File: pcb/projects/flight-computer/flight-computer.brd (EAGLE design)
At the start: 101.6 x 60.6 mm, 83 parts, among them IC1 ADG609RU, IC3 ADG609RU, P1 53048-0810, P2 53048-0810, U1 MCP73831/OT, U12 MAX31856MUD+, U13 MAX31856MUD+, U2 LP2985IM5-1.8/NOPB, U3 COM-13909, U4 ADXL377, U5 ICM-20948, U6 PCA9306DCUR, U7 SN74LVC1T45DRLR, U8 SN74LVC1T45DRLR, U9 DMP3099L

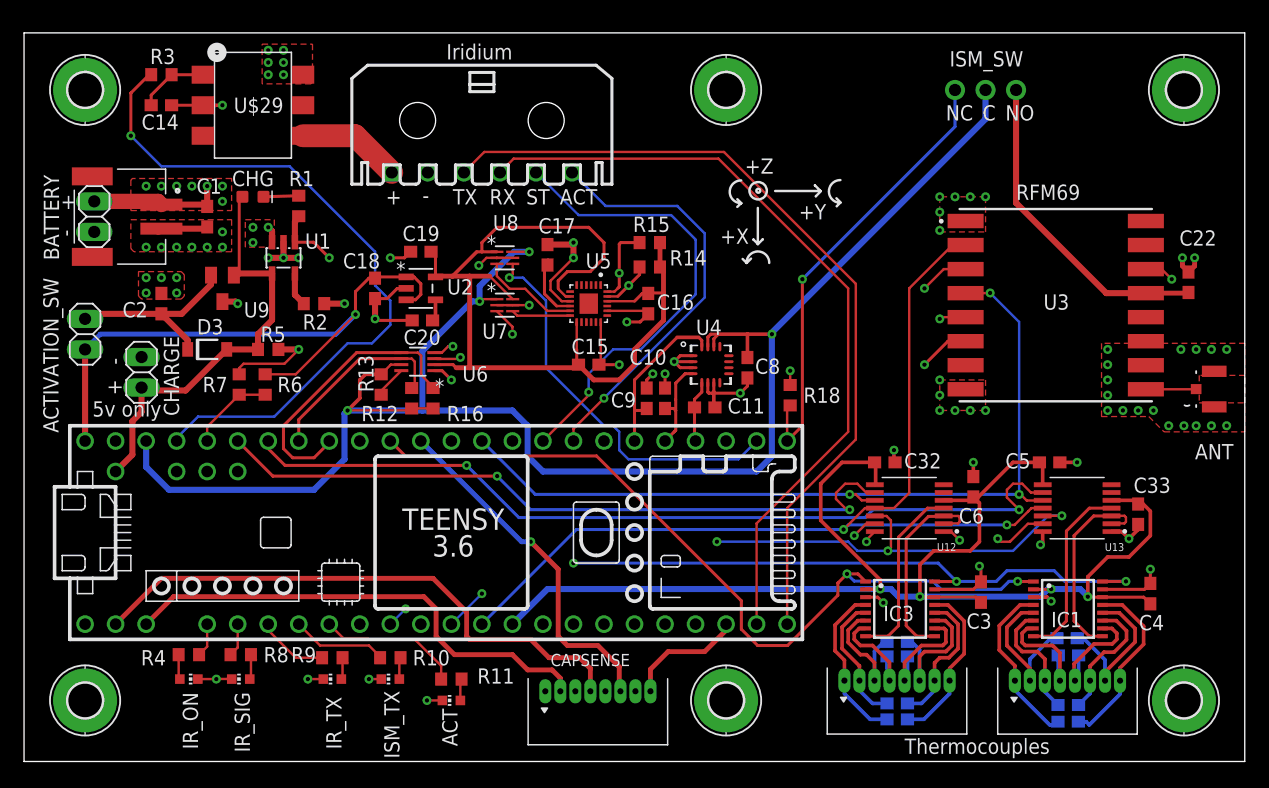
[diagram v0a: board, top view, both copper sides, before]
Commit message: add activation redundancy processor
- partial update of documentation to reflect this addition
- extra diagram of redundant activation
- pcb update to include a 32 pin qfn samd21 cortex m0 processor and necessary connections to bootload and flash over USB
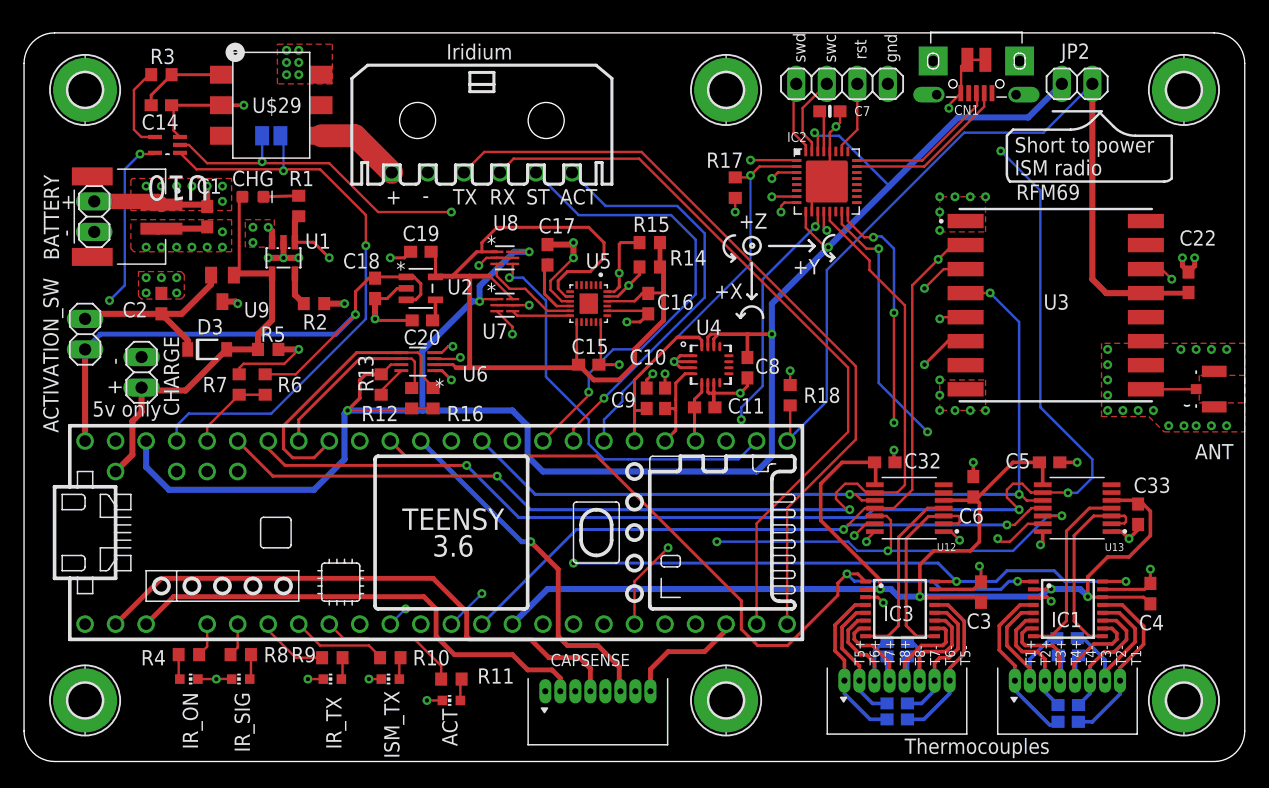
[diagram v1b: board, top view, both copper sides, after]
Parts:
- removed ISM_SW: (no value), adafruit:1X03-CLEANBIG
- added C7: 1uF, microbuilder:0603-NO
- added CN1: 4U#20329, microbuilder:4UCONN_20329_V2
- added IC2: ATSAMD21E, microbuilder:QFN32_5MM
- added JP1: (no value), pinhead:1X04
- added JP2: (no value), pinhead:1X02
- added R17: 470, rcl:R0603
- added SJ1: (no value), jumper:SJ
- added U10: SN74LVC1G08DCKR, SN74LVC1G08DCKR:SOT65P210X110-5N
- moved U$29 1.52 mm to (20.6, 54.6)
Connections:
- removed net RADIO_OFF_SIG: ISM_SW.1, R18.1, U$1.33/A14
- new net !RESET: IC2.26, JP1.3
- new net D+: CN1.D+, IC2.24
- new net D-: CN1.D-, IC2.23
- new net PRI_ACT: SJ1.1, U$1.23/A9, U10.1
- new net SEC_ACT: IC2.1, SJ1.2, U10.2
- new net SEC_CS: IC2.11, U$1.27
- new net SEC_EN: IC2.2, R17.1, U$1.39/A20
- new net SWCLK: IC2.31, JP1.2
- new net SWDIO: IC2.32, JP1.1
- new net VBUS: CN1.VBUS
- new net VDDCORE1: C7.1, IC2.29
- net 3V3: now also IC2.30, IC2.9, JP2.1, U10.5; no longer ISM_SW.2
- net 3V3_RADIO: now also JP2.2, R18.1, U$1.33/A14; no longer ISM_SW.3
- net ACT: now also U10.4; no longer U$1.23/A9
- net CS@TC1: now also IC2.3
- net CS@TC2: now also IC2.13
- net GND: now also C7.2, CN1.BASE@1, CN1.BASE@2, CN1.GND, CN1.SPRT@1, CN1.SPRT@2, CN1.SPRT@3, CN1.SPRT@4, IC2.10, IC2.28, IC2.33, JP1.4, R17.2, U10.3
- net MISO: now also IC2.12
- net MOSI: now also IC2.7
- net SCLK: now also IC2.8
- net TC1_FAULT: now also IC2.15
- net TC2_FAULT: now also IC2.16
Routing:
- net CS@TC1: track 71.3 -> 129.7 mm, vias 2 -> 5
- net SEC_ACT: track 0.00 -> 57.8 mm, vias 0 -> 3
- net ACT: track 58.7 -> 7.27 mm, vias 1 -> 0
- net PRI_ACT: track 0.00 -> 50.1 mm, vias 0 -> 2
- net 3V3: track 265.1 -> 312.8 mm, vias 8 -> 12
- net 3V3_RADIO: track 26.9 -> 71.9 mm
- net SEC_CS: track 0.00 -> 40.6 mm, vias 0 -> 3
- net RADIO_OFF_SIG: track 38.1 -> 0.00 mm, vias 1 -> 0
- net TC1_FAULT: track 46.2 -> 82.0 mm, vias 1 -> 3
- net TC2_FAULT: track 28.2 -> 61.2 mm, vias 1 -> 4
- net SEC_EN: track 0.00 -> 32.6 mm, vias 0 -> 1
- net CS@TC2: track 59.2 -> 87.3 mm
- net SCLK: track 70.8 -> 93.2 mm, vias 3 -> 4
- net GND: track 110.0 -> 131.3 mm, vias 78 -> 81
- net MOSI: track 93.2 -> 112.1 mm, vias 5 -> 6
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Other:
- outline, holes or cut-outs redrawn
- board text added: "KREPE Flight Computer V1.1 University of Kentucky 2020 Dr. Alexandre Martin, Dr. Bill Smith, Tyler Nichols, Matt Ruffner, Josh Laredo, Kirsten Ford, Andrew Perry"
- board text added: "Short for single activation source"
- board text added: "Short to power ISM radio"
- board text added: "T1+ T2+ T3+ T4+ T4- T3- T2- T1-"
- board text added: "T5+ T6+ T7+ T8+ T8- T7- T6- T5-"
- board text added: "gnd"
- board text added: "rst"
- board text added: "swc"
- board text added: "swd"
- board text removed: "KREPE Flight Computer V1.1 University of Kentucky 2020"

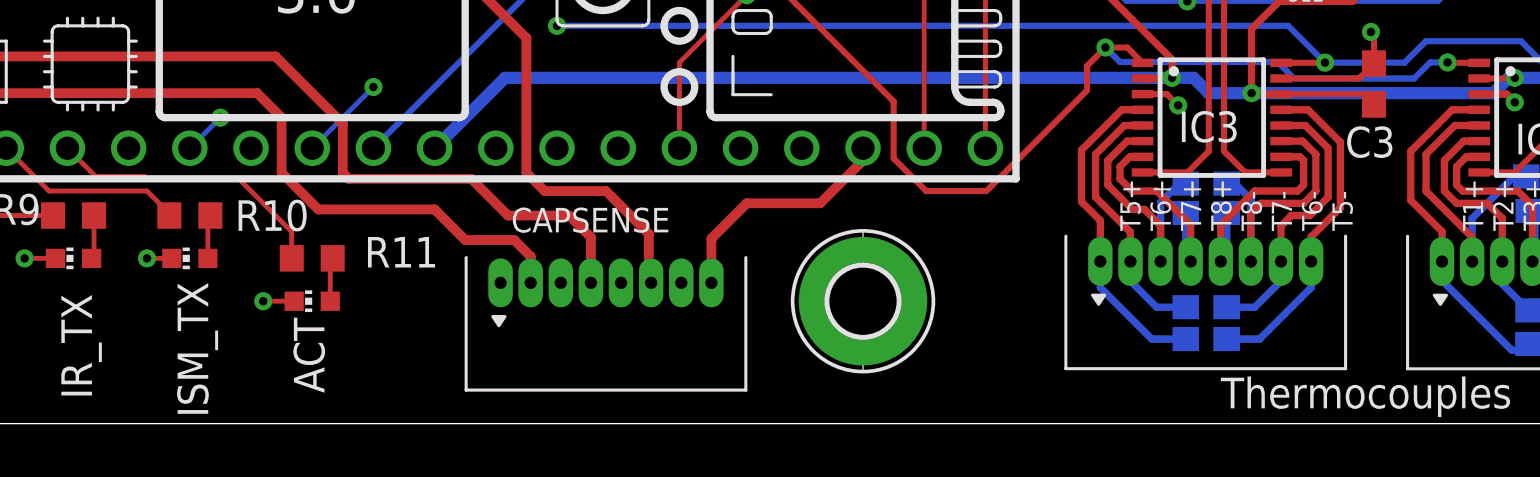
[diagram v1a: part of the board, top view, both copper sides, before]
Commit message: updated documentation, BOM and pinmap for activation redundancy processor
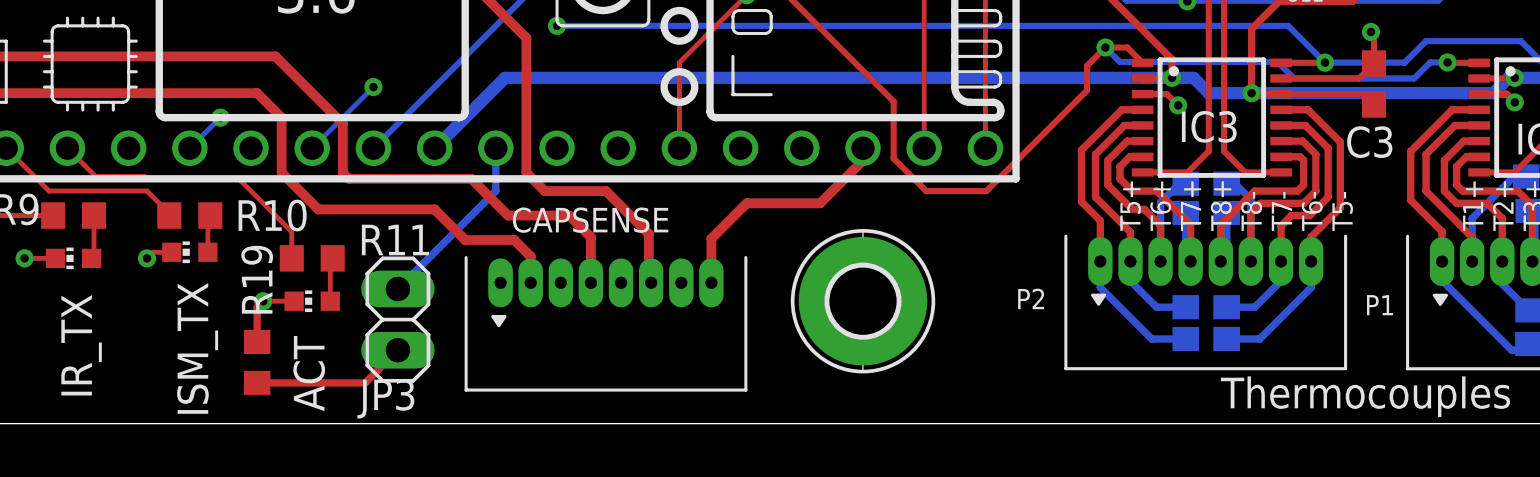
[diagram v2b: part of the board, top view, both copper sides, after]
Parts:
- added JP3: (no value), pinhead:1X02
- added R19: 100, rcl:R0603
- R17: value 470 -> 10k
- moved LED4 0.25 mm to (30.5, 7.11)
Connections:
- new net BUZZER: JP3.1, U$1.24
- new net N$2: JP3.2, R19.2
- net GND: now also R19.1
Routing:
- net BUZZER: track 0.00 -> 7.53 mm
- net N$2: track 0.00 -> 6.40 mm
- net GND: track 131.3 -> 133.2 mm
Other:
- board text added: "Buzzer + Buzzer -"
- board text added: "ISM Power Switch"
- board text added: "P1"
- board text added: "P2"
- board text removed: "C"
- board text removed: "NC"
- board text removed: "NO"
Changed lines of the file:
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@@
 <layer number="13" name="Route13" color="21" fill="1" visible="no" active="no"/>
 <layer number="14" name="Route14" color="22" fill="1" visible="no" active="no"/>
-<layer number="15" name="Route15" color="23" fill="1" visible="no" active="yes"/>
-<layer number="16" name="Bottom" color="1" fill="1" visible="no" active="yes"/>
+<layer number="15" name="Route15" color="23" fill="1" visible="yes" active="yes"/>
+<layer number="16" name="Bottom" color="1" fill="1" visible="yes" active="yes"/>
 <layer number="17" name="Pads" color="2" fill="1" visible="yes" active="yes"/>
 <layer number="18" name="Vias" color="2" fill="1" visible="yes" active="yes"/>
@@
 <layer number="24" name="bOrigins" color="15" fill="1" visible="no" active="yes"/>
 <layer number="25" name="tNames" color="7" fill="1" visible="yes" active="yes"/>
-<layer number="26" name="bNames" color="7" fill="1" visible="no" active="yes"/>
+<layer number="26" name="bNames" color="7" fill="1" visible="yes" active="yes"/>
 <layer number="27" name="tValues" color="7" fill="1" visible="no" active="yes"/>
 <layer number="28" name="bValues" color="7" fill="1" visible="no" active="yes"/>
@@
 <text x="82.423" y="48.768" size="1.27" layer="25">Short to power
 ISM radio</text>
-<text x="78.486" y="53.34" size="1.27" layer="26" rot="MR0">NC</text>
-<text x="80.391" y="53.34" size="1.27" layer="26" rot="MR0">C</text>
-<text x="83.566" y="53.34" size="1.27" layer="26" rot="MR0">NO</text>
+<text x="92.964" y="53.086" size="1.016" layer="26" rot="MR0">ISM Power Switch</text>
 <text x="63.5762" y="14.025878125" size="1.397" layer="26" rot="MR0">KREPE Flight Computer V1.1
 University of Kentucky 2020
@@
 <text x="26.416" y="1.016" size="1.27" layer="25" rot="R90">IR_TX</text>
 <text x="31.242" y="0.254" size="1.27" layer="25" rot="R90">ISM_TX</text>
-<text x="36.068" y="1.27" size="1.27" layer="25" rot="R90">ACT</text>
+<text x="36.068" y="0.508" size="1.27" layer="25" rot="R90">ACT</text>
 <wire x1="61.991240625" y1="42.9006" x2="65.775840625" y2="42.9006" width="0.2032" layer="25"/>
 <wire x1="65.775840625" y1="42.9006" x2="65.78091875" y2="42.895521875" width="0.2032" layer="25"/>
@@
 <text x="58.928" y="50.546" size="1.27" layer="26" rot="MR0">Net Name</text>
 <text x="89.662" y="50.546" size="1.27" layer="26" rot="MR0">Net Name</text>
-<text x="39.624" y="8.89" size="1.27" layer="26" rot="MR0">Cap.Ch.3</text>
-<text x="39.624" y="7.112" size="1.27" layer="26" rot="MR0">Cap.Ch.2</text>
-<text x="39.624" y="1.016" size="1.27" layer="26" rot="MR0">Cap.Ch.0</text>
-<text x="39.624" y="3.302" size="1.27" layer="26" rot="MR0">Cap.Ch.1</text>
-<wire x1="39.878" y1="9.398" x2="52.07" y2="9.398" width="0.2032" layer="26"/>
+<text x="48.514" y="9.398" size="1.27" layer="26" rot="MR0">Cap.Ch.3</text>
+<text x="48.26" y="7.874" size="1.27" layer="26" rot="MR0">Cap.Ch.2</text>
+<text x="56.134" y="1.27" size="1.27" layer="26" rot="MR0">Cap.Ch.0</text>
+<text x="55.118" y="3.048" size="1.27" layer="26" rot="MR0">Cap.Ch.1</text>
+<wire x1="49.022" y1="9.398" x2="52.07" y2="9.398" width="0.2032" layer="26"/>
 <wire x1="52.07" y1="9.398" x2="52.07" y2="7.112" width="0.2032" layer="26"/>
-<wire x1="40.132" y1="7.874" x2="49.657" y2="7.874" width="0.2032" layer="26"/>
+<wire x1="49.022" y1="7.874" x2="49.657" y2="7.874" width="0.2032" layer="26"/>
 <wire x1="49.657" y1="7.874" x2="49.657" y2="7.112" width="0.2032" layer="26"/>
-<wire x1="40.386" y1="1.524" x2="47.117" y2="1.651" width="0.2032" layer="26"/>
-<wire x1="47.117" y1="1.651" x2="47.117" y2="4.445" width="0.2032" layer="26"/>
-<wire x1="39.878" y1="3.556" x2="44.577" y2="3.556" width="0.2032" layer="26"/>
+<wire x1="48.26" y1="1.651" x2="46.863" y2="1.651" width="0.2032" layer="26"/>
+<wire x1="46.863" y1="1.651" x2="46.863" y2="4.445" width="0.2032" layer="26"/>
+<wire x1="47.498" y1="3.556" x2="44.577" y2="3.556" width="0.2032" layer="26"/>
 <wire x1="44.577" y1="3.556" x2="44.577" y2="4.318" width="0.2032" layer="26"/>
 <text x="3.048" y="45.974" size="1.27" layer="25">+</text>
@@
 T5-
 </text>
+<text x="66.04" y="5.588" size="0.8382" layer="25" font="vector" rot="R180">P2</text>
+<text x="80.518" y="5.334" size="0.8382" layer="25" font="vector" rot="R180">P1</text>
+<text x="37.084" y="3.048" size="1.143" layer="26" rot="MR0">Buzzer +
+Buzzer -</text>
 </plain>
 <attributes>
@@
 <attribute name="VALUE" x="26.289" y="8.763" size="1.27" layer="27" rot="R180"/>
 </element>
-<element name="LED4" library="adafruit" library_urn="urn:adsk.eagle:library:420" package="CHIP-LED0603" package3d_urn="urn:adsk.eagle:package:6240556/1" value="" x="30.48" y="6.858" smashed="yes" rot="R90">
-<attribute name="VALUE" x="31.115" y="8.763" size="1.27" layer="27" rot="R180"/>
+<element name="LED4" library="adafruit" library_urn="urn:adsk.eagle:library:420" package="CHIP-LED0603" package3d_urn="urn:adsk.eagle:package:6240556/1" value="" x="30.48" y="7.112" smashed="yes" rot="R90">
+<attribute name="VALUE" x="31.115" y="9.017" size="1.27" layer="27" rot="R180"/>
 </element>
 <element name="LED5" library="adafruit" library_urn="urn:adsk.eagle:library:420" package="CHIP-LED0603" package3d_urn="urn:adsk.eagle:package:6240556/1" value="" x="35.56" y="5.08" smashed="yes" rot="R90">
@@
 </element>
 <element name="R11" library="rcl" library_urn="urn:adsk.eagle:library:334" package="R0603" package3d_urn="urn:adsk.eagle:package:23555/3" value="470" x="35.56" y="6.858" smashed="yes">
-<attribute name="NAME" x="37.719" y="6.477" size="1.27" layer="25"/>
+<attribute name="NAME" x="37.465" y="6.985" size="1.27" layer="25"/>
 <attribute name="POPULARITY" value="77" x="35.56" y="6.858" size="1.778" layer="27" display="off"/>
 <attribute name="SPICEPREFIX" value="R" x="35.56" y="6.858" size="1.778" layer="27" display="off"/>
@@
 <attribute name="VALUE" x="20.1739" y="52.07" size="0.02" layer="28" rot="MR0"/>
 </element>
-<element name="R17" library="rcl" library_urn="urn:adsk.eagle:library:334" package="R0603" package3d_urn="urn:adsk.eagle:package:23555/3" value="470" x="59.182" y="47.752" smashed="yes" rot="R270">
+<element name="R17" library="rcl" library_urn="urn:adsk.eagle:library:334" package="R0603" package3d_urn="urn:adsk.eagle:package:23555/3" value="10k" x="59.182" y="47.752" smashed="yes" rot="R270">
 <attribute name="NAME" x="56.769" y="49.403" size="1.27" layer="25"/>
 <attribute name="POPULARITY" value="77" x="59.182" y="47.752" size="1.143" layer="27" font="vector" rot="R270" display="off"/>
@@
 <attribute name="VALUE" x="57.277" y="48.387" size="1.27" layer="27" rot="R270"/>
 </element>
+<element name="JP3" library="pinhead" package="1X02" package3d_urn="urn:adsk.eagle:package:22435/2" value="" x="39.116" y="4.318" smashed="yes" rot="R270">
+<attribute name="NAME" x="37.5158" y="0.5588" size="1.27" layer="25" ratio="10"/>
+<attribute name="POPULARITY" value="98" x="39.116" y="4.318" size="1.778" layer="27" rot="R270" display="off"/>
+<attribute name="VALUE" x="35.941" y="6.858" size="1.27" layer="27" rot="R270"/>
+</element>
+<element name="R19" library="rcl" library_urn="urn:adsk.eagle:library:334" package="R0603" package3d_urn="urn:adsk.eagle:package:23555/3" value="100" x="33.274" y="2.54" smashed="yes" rot="R270">
+<attribute name="NAME" x="32.639" y="7.493" size="1.27" layer="25" rot="R270"/>
+<attribute name="POPULARITY" value="77" x="33.274" y="2.54" size="1.778" layer="27" rot="R270" display="off"/>
+<attribute name="SPICEPREFIX" value="R" x="33.274" y="2.54" size="1.778" layer="27" rot="R270" display="off"/>
+<attribute name="VALUE" x="31.369" y="3.175" size="1.27" layer="27" rot="R270"/>
+</element>
 </elements>
 <signals>
@@
 <wire x1="24.904" y1="6.858" x2="23.622" y2="6.858" width="0.2032" layer="1"/>
 <via x="23.622" y="6.858" extent="1-16" drill="0.35"/>
-<wire x1="29.73" y1="6.858" x2="28.702" y2="6.858" width="0.2032" layer="1"/>
+<wire x1="29.73" y1="7.112" x2="28.956" y2="7.112" width="0.2032" layer="1"/>
+<wire x1="28.956" y1="7.112" x2="28.702" y2="6.858" width="0.2032" layer="1"/>
 <via x="28.702" y="6.858" extent="1-16" drill="0.35"/>
 <via x="33.528" y="5.08" extent="1-16" drill="0.35"/>
@@
 <via x="59.182" y="45.72" extent="1-16" drill="0.35"/>
 <wire x1="59.182" y1="46.902" x2="59.182" y2="45.72" width="0.2032" layer="1"/>
+<contactref element="R19" pad="1"/>
+<wire x1="33.274" y1="3.39" x2="33.274" y2="4.826" width="0.3048" layer="1"/>
+<wire x1="33.274" y1="4.826" x2="33.528" y2="5.08" width="0.3048" layer="1"/>
 <wire x1="82.548" y1="55.488" x2="82.848" y2="58.288" width="0" layer="19" extent="1-1"/>
 <wire x1="75.648" y1="58.288" x2="75.948" y2="55.488" width="0" layer="19" extent="1-1"/>
@@
 <contactref element="LED4" pad="A"/>
 <wire x1="31.33" y1="8.636" x2="31.23" y2="8.536" width="0.2032" layer="1"/>
-<wire x1="31.23" y1="8.536" x2="31.23" y2="6.858" width="0.2032" layer="1"/>
+<wire x1="31.23" y1="8.536" x2="31.23" y2="7.112" width="0.2032" layer="1"/>
 </signal>
 <signal name="N$28">
@@
 <contactref element="CN1" pad="VBUS"/>
 </signal>
+<signal name="BUZZER">
+<contactref element="U$1" pad="24"/>
+<contactref element="JP3" pad="1"/>
+<wire x1="43.18" y1="11.43" x2="43.18" y2="9.652" width="0.3048" layer="16"/>
+<wire x1="43.18" y1="9.652" x2="39.116" y2="5.588" width="0.3048" layer="16"/>
+</signal>
+<signal name="N$2">
+<contactref element="JP3" pad="2"/>
+<contactref element="R19" pad="2"/>
+<wire x1="33.274" y1="1.69" x2="37.758" y2="1.69" width="0.3048" layer="1"/>
+<wire x1="37.758" y1="1.69" x2="39.116" y2="3.048" width="0.3048" layer="1"/>
+</signal>
 </signals>
